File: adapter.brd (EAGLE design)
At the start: 21.6 x 19 mm, 5 parts

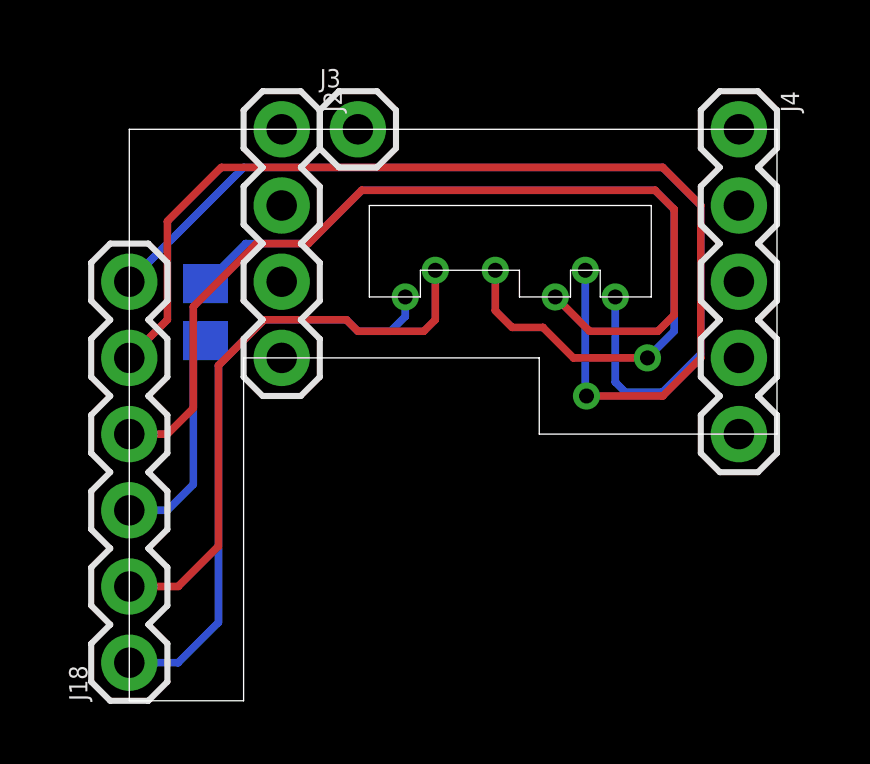
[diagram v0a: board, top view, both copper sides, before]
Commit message: adapter fix
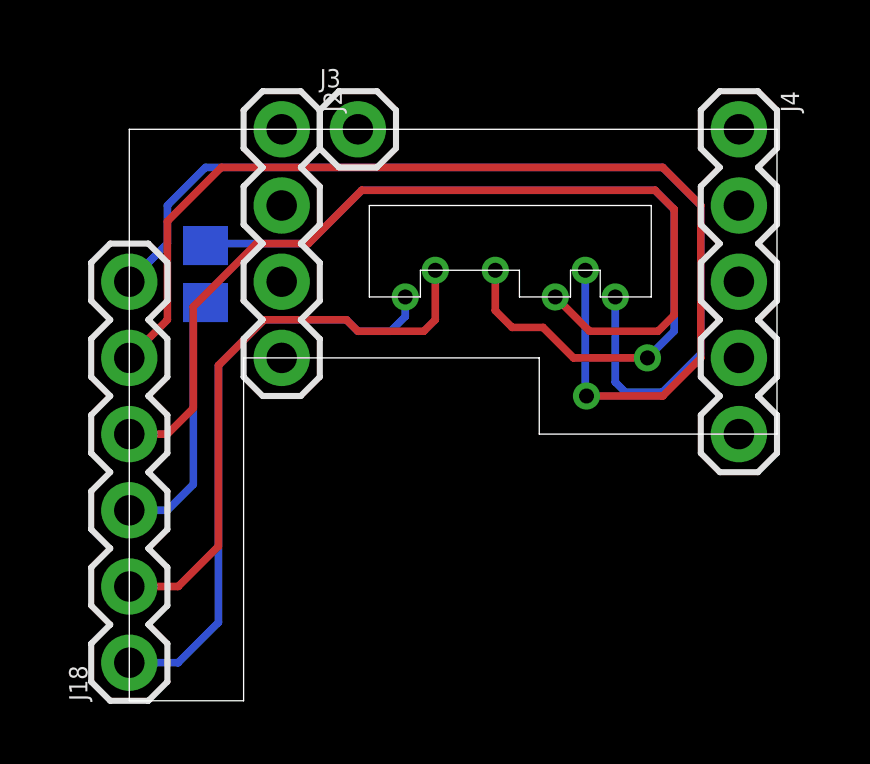
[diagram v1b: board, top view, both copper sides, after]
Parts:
- moved R1 1.27 mm to (-2.54, 1.52)
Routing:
- net N$1: track 7.45 -> 8.72 mm
- net SD_DAT2: track 32.5 -> 33.2 mm
- net SD_CLK: track 29.6 -> 29.0 mm
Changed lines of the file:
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@@
 <attribute name="PROD_ID" value="CONN-09696" x="0" y="6.35" size="1.778" layer="27" rot="R270" display="off"/>
 </element>
-<element name="R1" library="rcl" package="R0805" value="33" x="-2.54" y="0.254" rot="MR90"/>
+<element name="R1" library="rcl" package="R0805" value="33" x="-2.54" y="1.524" rot="MR90"/>
 </elements>
 <signals>
@@
 <wire x1="13.97" y1="-1.13666875" x2="13.97" y2="3.81" width="0.254" layer="16"/>
 <wire x1="13.97" y1="3.81" x2="12.7" y2="5.08" width="0.254" layer="16"/>
-<wire x1="12.7" y1="5.08" x2="-1.27" y2="5.08" width="0.254" layer="16"/>
-<wire x1="-1.27" y1="5.08" x2="-5.08" y2="1.27" width="0.254" layer="16"/>
+<wire x1="12.7" y1="5.08" x2="-2.54" y2="5.08" width="0.254" layer="16"/>
+<wire x1="-2.54" y1="5.08" x2="-3.81" y2="3.81" width="0.254" layer="16"/>
+<wire x1="-3.81" y1="3.81" x2="-3.81" y2="2.54" width="0.254" layer="16"/>
+<wire x1="-3.81" y1="2.54" x2="-5.08" y2="1.27" width="0.254" layer="16"/>
 </signal>
 <signal name="SD_DAT1">
@@
 <signal name="SD_CLK">
 <via x="7.12" y="1.651" extent="1-16" drill="0.5"/>
-<wire x1="0.889" y1="2.54" x2="-1.204" y2="2.54" width="0.254" layer="16"/>
-<wire x1="-1.204" y1="2.54" x2="-2.54" y2="1.204" width="0.254" layer="16"/>
+<wire x1="0.889" y1="2.54" x2="-2.474" y2="2.54" width="0.254" layer="16"/>
+<wire x1="-2.474" y1="2.54" x2="-2.54" y2="2.474" width="0.254" layer="16"/>
 <wire x1="13.081" y1="-0.381" x2="13.081" y2="3.683" width="0.254" layer="16"/>
 <wire x1="13.081" y1="3.683" x2="12.446" y2="4.318" width="0.254" layer="16"/>
@@
 <contactref element="J18" pad="3"/>
 <contactref element="R1" pad="1"/>
-<wire x1="-2.9464" y1="-1.1024" x2="-2.9464" y2="-5.4864" width="0.254" layer="16"/>
+<wire x1="-2.9464" y1="0.1676" x2="-2.9464" y2="-5.4864" width="0.254" layer="16"/>
 <wire x1="-2.9464" y1="-5.4864" x2="-3.81" y2="-6.35" width="0.254" layer="16"/>
 <wire x1="-3.81" y1="-6.35" x2="-5.08" y2="-6.35" width="0.254" layer="16"/>
-<wire x1="-2.54" y1="-0.696" x2="-2.9464" y2="-1.1024" width="0.254" layer="16"/>
+<wire x1="-2.54" y1="0.574" x2="-2.9464" y2="0.1676" width="0.254" layer="16"/>
 </signal>
 </signals>
